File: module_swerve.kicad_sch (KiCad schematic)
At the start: 6 parts, among them J2 PlayingWFusion_CANDaisy_5-Link, M10 REV_NEO_Brushless_Motor, M11 REV_NEO_Brushless_Motor, U19 REV_Spark_MAX, U20 CTRE_CANCoder, U21 REV_Spark_MAX

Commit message: v1.2: added photoelectric sensor labels
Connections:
- new net: M11. (IN_C), U21. (VIN-)
- new net: M10. (IN_C), U19. (VIN-)
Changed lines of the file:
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@@
   (title_block
     (title "Schéma de câblage Disc-O 2024")
-    (date "2024-02-04")
-    (rev "1.1")
+    (date "2024-02-06")
+    (rev "1.2")
     (company "ASTRO 7605 (2024)")
   )

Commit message: Modify some fuses to 40A
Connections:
- new net: M11. (IN_C), U21. (VIN-)
- new net: M10. (IN_C), U19. (VIN-)
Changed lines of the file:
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@@
   (title_block
     (title "Schéma de câblage Disc-O 2024")
-    (date "2024-02-06")
-    (rev "1.2")
+    (date "2024-02-12")
+    (rev "1.4")
     (company "ASTRO 7605 (2024)")
   )

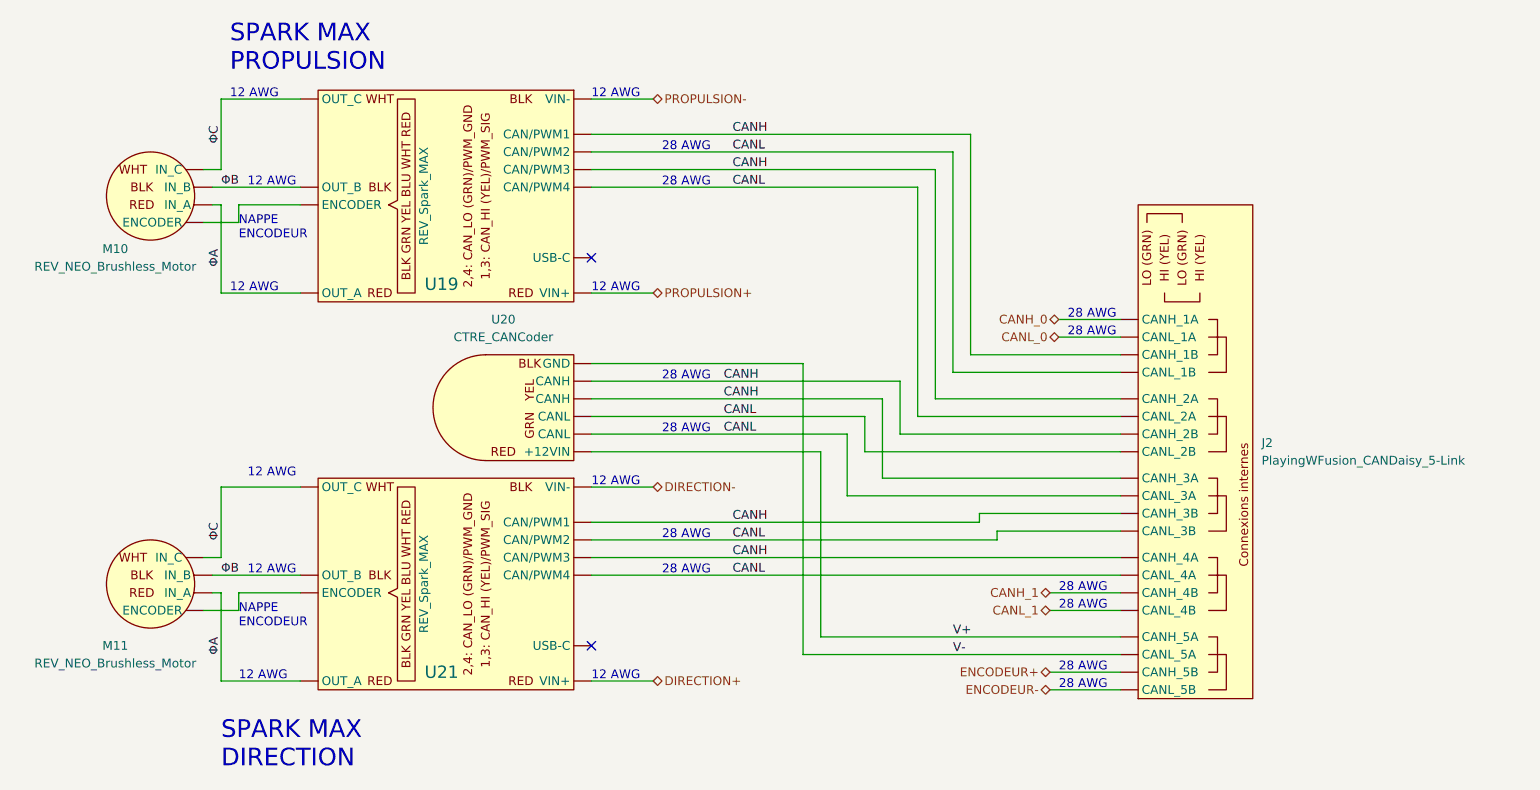
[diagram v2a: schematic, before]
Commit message: Ajout Orange Pi + sous-systeme vision
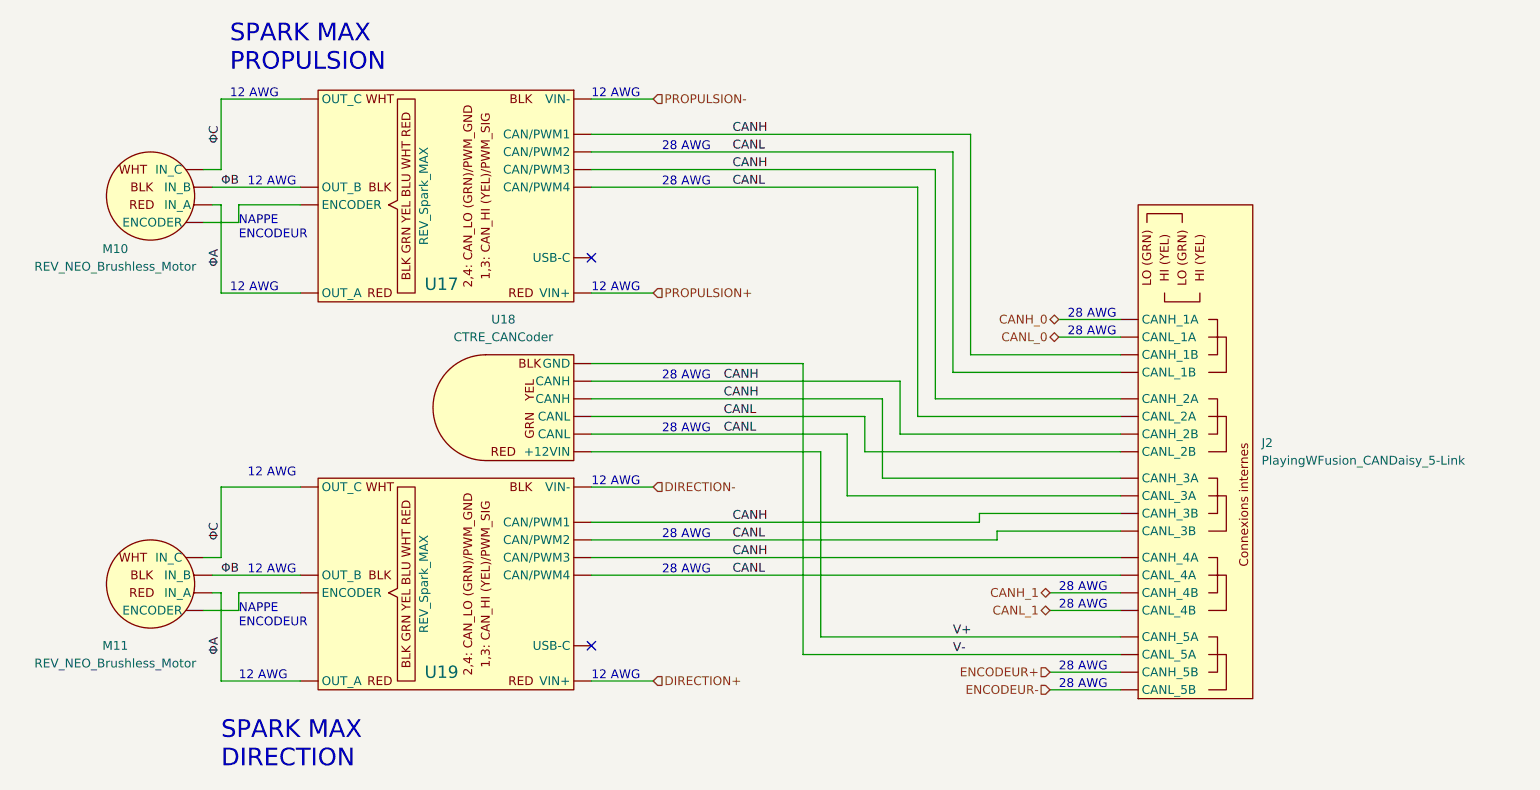
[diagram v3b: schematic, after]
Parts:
- renumbered U19 to U17, U20 to U18, U21 to U19
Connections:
- new net: M11. (IN_C), U19. (VIN-)
- new net: M10. (IN_C), U17. (VIN-)
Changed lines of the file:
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@@
   (title_block
     (title "Schéma de câblage Disc-O 2024")
-    (date "2024-02-12")
-    (rev "1.4")
+    (date "2024-02-17")
+    (rev "1.5")
     (company "ASTRO 7605 (2024)")
   )
@@
     (effects (font (size 1.27 1.27)) (justify left bottom))
   )
-  (hierarchical_label "ENCODEUR+" (shape bidirectional) (at 184.15 120.65 180) (fields_autoplaced)
+  (hierarchical_label "ENCODEUR+" (shape input) (at 184.15 120.65 180) (fields_autoplaced)
     (effects (font (size 1.27 1.27)) (justify right))
   )
-  (hierarchical_label "DIRECTION+" (shape bidirectional) (at 127 121.92 0) (fields_autoplaced)
+  (hierarchical_label "DIRECTION+" (shape input) (at 127 121.92 0) (fields_autoplaced)
     (effects (font (size 1.27 1.27)) (justify left))
   )
-  (hierarchical_label "PROPULSION+" (shape bidirectional) (at 127 66.04 0) (fields_autoplaced)
+  (hierarchical_label "PROPULSION+" (shape input) (at 127 66.04 0) (fields_autoplaced)
     (effects (font (size 1.27 1.27)) (justify left))
   )
@@
     (effects (font (size 1.27 1.27)) (justify right))
   )
-  (hierarchical_label "ENCODEUR-" (shape bidirectional) (at 184.15 123.19 180) (fields_autoplaced)
+  (hierarchical_label "ENCODEUR-" (shape input) (at 184.15 123.19 180) (fields_autoplaced)
     (effects (font (size 1.27 1.27)) (justify right))
   )
-  (hierarchical_label "PROPULSION-" (shape bidirectional) (at 127 38.1 0) (fields_autoplaced)
+  (hierarchical_label "PROPULSION-" (shape input) (at 127 38.1 0) (fields_autoplaced)
     (effects (font (size 1.27 1.27)) (justify left))
   )
-  (hierarchical_label "DIRECTION-" (shape bidirectional) (at 127 93.98 0) (fields_autoplaced)
+  (hierarchical_label "DIRECTION-" (shape input) (at 127 93.98 0) (fields_autoplaced)
     (effects (font (size 1.27 1.27)) (justify left))
   )
   (symbol (lib_id "FRC_Components:CTRE_CANCoder") (at 96.52 82.55 90) (unit 1)
     (in_bom yes) (on_board yes) (dnp no)
-    (property "Reference" "U20" (at 105.4294 69.85 90)
+    (property "Reference" "U18" (at 105.4294 69.85 90)
       (effects (font (size 1.27 1.27)))
     )
@@
       (project "schema_cablage_2024"
         (path "/e63e39d7-6ac0-4ffd-8aa3-1841a4541b55/b632b64e-d5b7-456d-a7ae-6969aba14a97"
-          (reference "U20") (unit 1)
+          (reference "U18") (unit 1)
         )
         (path "/e63e39d7-6ac0-4ffd-8aa3-1841a4541b55/e92e2da7-8df4-42ea-b0b1-e2a2f3556d07"
-          (reference "U29") (unit 1)
+          (reference "U27") (unit 1)
         )
         (path "/e63e39d7-6ac0-4ffd-8aa3-1841a4541b55/e4b49782-05fc-4e80-9ba9-edd7f0cdce32"
-          (reference "U23") (unit 1)
+          (reference "U21") (unit 1)
         )
         (path "/e63e39d7-6ac0-4ffd-8aa3-1841a4541b55/3439eb03-35bd-48b7-a9f1-5d73cc12bdd7"
-          (reference "U26") (unit 1)
+          (reference "U24") (unit 1)
         )
       )
@@
       (effects (font (size 1.27 1.27)) hide)
     )
-    (property "Datasheet" "" (at 69.85 107.95 0)
+    (property "Datasheet" "https://www.revrobotics.com/rev-21-1650/" (at 69.85 107.95 0)
       (effects (font (size 1.27 1.27)) hide)
     )
@@
   (symbol (lib_id "FRC_Components:REV_Spark_MAX") (at 96.52 52.07 270) (unit 1)
     (in_bom yes) (on_board yes) (dnp no)
-    (property "Reference" "U19" (at 96.52 64.77 90)
+    (property "Reference" "U17" (at 96.52 64.77 90)
       (effects (font (size 1.778 1.778)))
     )
@@
       (effects (font (size 1.27 1.27)) hide)
     )
-    (property "Datasheet" "" (at 96.52 52.07 0)
+    (property "Datasheet" "https://docs.revrobotics.com/brushless/spark-max/overview" (at 96.52 52.07 0)
+      (effects (font (size 1.27 1.27)) hide)
+    )
+    (pin "")
+    (pin "")
+    (pin "")
+    (pin "")
+    (pin "")
+    (pin "")
+    (pin "")
+    (pin "")
+    (pin "")
+    (pin "")
+    (pin "")
+    (instances
+      (project "schema_cablage_2024"
+        (path "/e63e39d7-6ac0-4ffd-8aa3-1841a4541b55/b632b64e-d5b7-456d-a7ae-6969aba14a97"
+          (reference "U17") (unit 1)
+        )
+        (path "/e63e39d7-6ac0-4ffd-8aa3-1841a4541b55/e4b49782-05fc-4e80-9ba9-edd7f0cdce32"
+          (reference "U20") (unit 1)
+        )
+        (path "/e63e39d7-6ac0-4ffd-8aa3-1841a4541b55/3439eb03-35bd-48b7-a9f1-5d73cc12bdd7"
+          (reference "U23") (unit 1)
+        )
+        (path "/e63e39d7-6ac0-4ffd-8aa3-1841a4541b55/e92e2da7-8df4-42ea-b0b1-e2a2f3556d07"
+          (reference "U26") (unit 1)
+        )
+      )
+    )
+  )
+  (symbol (lib_id "FRC_Components:REV_Spark_MAX") (at 96.52 107.95 270) (unit 1)
+    (in_bom yes) (on_board yes) (dnp no)
+    (property "Reference" "U19" (at 96.52 120.65 90)
+      (effects (font (size 1.778 1.778)))
+    )
+    (property "Value" "REV_Spark_MAX" (at 93.98 107.95 0)
+      (effects (font (size 1.27 1.27)))
+    )
+    (property "Footprint" "" (at 96.52 107.95 0)
+      (effects (font (size 1.27 1.27)) hide)
+    )
+    (property "Datasheet" "https://docs.revrobotics.com/brushless/spark-max/overview" (at 96.52 107.95 0)
       (effects (font (size 1.27 1.27)) hide)
     )
@@
     )
   )
-  (symbol (lib_id "FRC_Components:REV_Spark_MAX") (at 96.52 107.95 270) (unit 1)
-    (in_bom yes) (on_board yes) (dnp no)
-    (property "Reference" "U21" (at 96.52 120.65 90)
-      (effects (font (size 1.778 1.778)))
-    )
-    (property "Value" "REV_Spark_MAX" (at 93.98 107.95 0)
-      (effects (font (size 1.27 1.27)))
-    )
-    (property "Footprint" "" (at 96.52 107.95 0)
-      (effects (font (size 1.27 1.27)) hide)
-    )
-    (property "Datasheet" "" (at 96.52 107.95 0)
-      (effects (font (size 1.27 1.27)) hide)
-    )
-    (pin "")
-    (pin "")
-    (pin "")
-    (pin "")
-    (pin "")
-    (pin "")
-    (pin "")
-    (pin "")
-    (pin "")
-    (pin "")
-    (pin "")
-    (instances
-      (project "schema_cablage_2024"
-        (path "/e63e39d7-6ac0-4ffd-8aa3-1841a4541b55/b632b64e-d5b7-456d-a7ae-6969aba14a97"
-          (reference "U21") (unit 1)
-        )
-        (path "/e63e39d7-6ac0-4ffd-8aa3-1841a4541b55/e4b49782-05fc-4e80-9ba9-edd7f0cdce32"
-          (reference "U24") (unit 1)
-        )
-        (path "/e63e39d7-6ac0-4ffd-8aa3-1841a4541b55/3439eb03-35bd-48b7-a9f1-5d73cc12bdd7"
-          (reference "U27") (unit 1)
-        )
-        (path "/e63e39d7-6ac0-4ffd-8aa3-1841a4541b55/e92e2da7-8df4-42ea-b0b1-e2a2f3556d07"
-          (reference "U30") (unit 1)
-        )
-      )
-    )
-  )
   (symbol (lib_id "FRC_Components:PlayingWFusion_CANDaisy_5-Link") (at 187.96 88.9 90) (unit 1)
     (in_bom yes) (on_board yes) (dnp no) (fields_autoplaced)
@@
       (effects (font (size 1.27 1.27)) hide)
     )
-    (property "Datasheet" "" (at 69.85 52.07 0)
-      (effects (font (size 1.27 1.27)) hide)
-    )
+    (property "Datasheet" "https://www.revrobotics.com/rev-21-1650/" (at 69.85 52.07 0)
+      (effects (font (size 1.27 1.27)) hide)
+    )

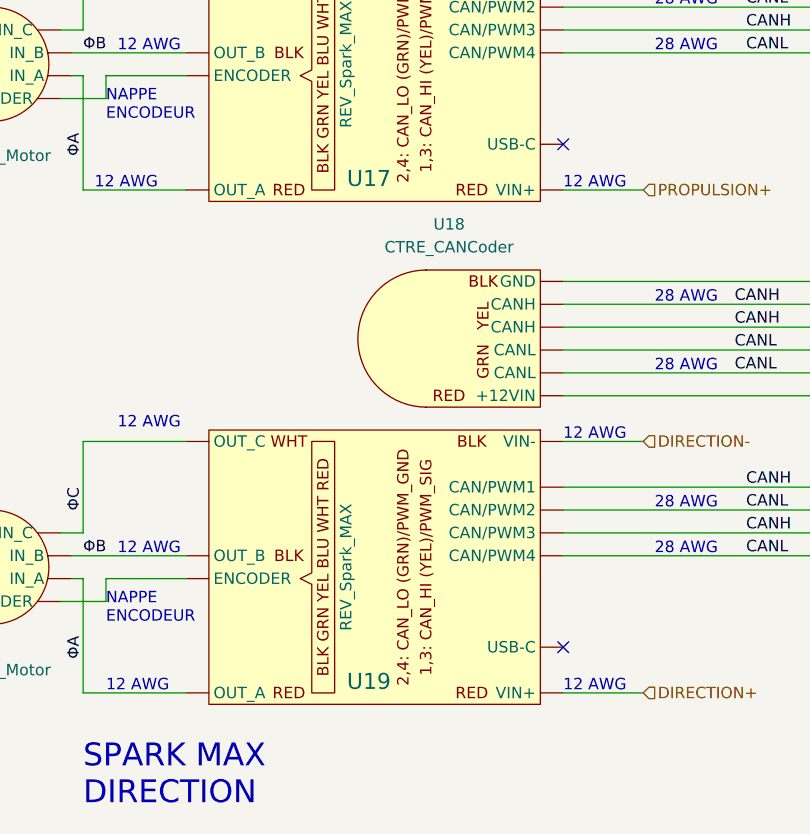
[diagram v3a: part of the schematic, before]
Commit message: Ajout Limelight + webcam
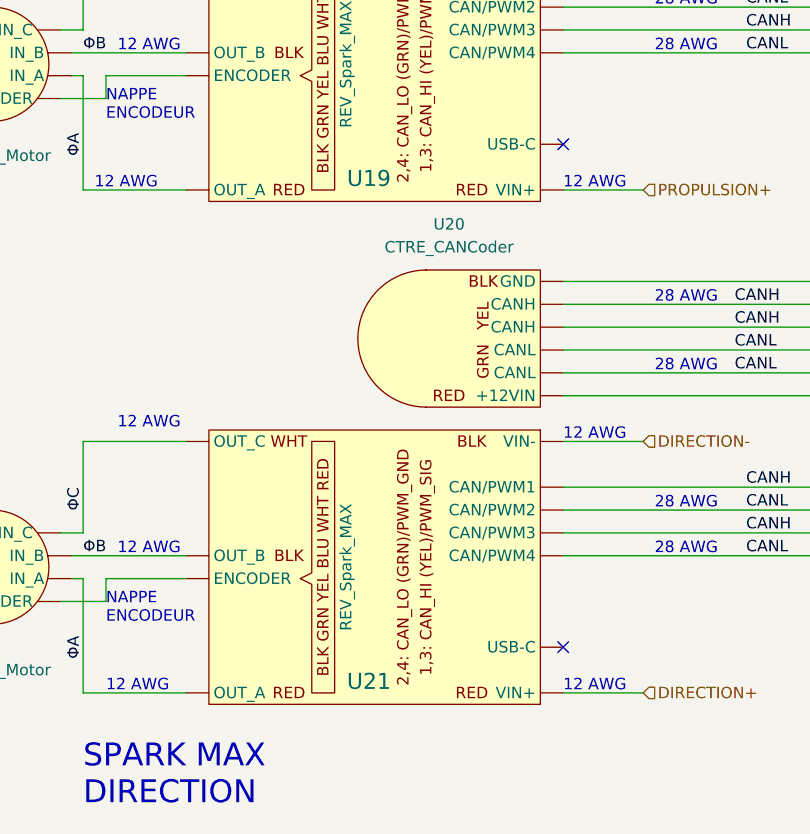
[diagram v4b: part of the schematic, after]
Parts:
- renumbered U17 to U19, U18 to U20, U19 to U21
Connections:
- new net: M11. (IN_C), U21. (VIN-)
- new net: M10. (IN_C), U19. (VIN-)
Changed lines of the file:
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@@
   (title_block
     (title "Schéma de câblage Disc-O 2024")
-    (date "2024-02-17")
-    (rev "1.5")
+    (date "2024-02-27")
+    (rev "1.6")
     (company "ASTRO 7605 (2024)")
   )
@@
   (symbol (lib_id "FRC_Components:CTRE_CANCoder") (at 96.52 82.55 90) (unit 1)
     (in_bom yes) (on_board yes) (dnp no)
-    (property "Reference" "U18" (at 105.4294 69.85 90)
+    (property "Reference" "U20" (at 105.4294 69.85 90)
       (effects (font (size 1.27 1.27)))
     )
@@
       (project "schema_cablage_2024"
         (path "/e63e39d7-6ac0-4ffd-8aa3-1841a4541b55/b632b64e-d5b7-456d-a7ae-6969aba14a97"
-          (reference "U18") (unit 1)
+          (reference "U20") (unit 1)
         )
         (path "/e63e39d7-6ac0-4ffd-8aa3-1841a4541b55/e92e2da7-8df4-42ea-b0b1-e2a2f3556d07"
-          (reference "U27") (unit 1)
+          (reference "U29") (unit 1)
         )
         (path "/e63e39d7-6ac0-4ffd-8aa3-1841a4541b55/e4b49782-05fc-4e80-9ba9-edd7f0cdce32"
-          (reference "U21") (unit 1)
+          (reference "U23") (unit 1)
         )
         (path "/e63e39d7-6ac0-4ffd-8aa3-1841a4541b55/3439eb03-35bd-48b7-a9f1-5d73cc12bdd7"
-          (reference "U24") (unit 1)
+          (reference "U26") (unit 1)
         )
       )
@@
   (symbol (lib_id "FRC_Components:REV_Spark_MAX") (at 96.52 52.07 270) (unit 1)
     (in_bom yes) (on_board yes) (dnp no)
-    (property "Reference" "U17" (at 96.52 64.77 90)
+    (property "Reference" "U19" (at 96.52 64.77 90)
       (effects (font (size 1.778 1.778)))
     )
@@
     )
     (property "Datasheet" "https://docs.revrobotics.com/brushless/spark-max/overview" (at 96.52 52.07 0)
-      (effects (font (size 1.27 1.27)) hide)
-    )
-    (pin "")
-    (pin "")
-    (pin "")
-    (pin "")
-    (pin "")
-    (pin "")
-    (pin "")
-    (pin "")
-    (pin "")
-    (pin "")
-    (pin "")
-    (instances
-      (project "schema_cablage_2024"
-        (path "/e63e39d7-6ac0-4ffd-8aa3-1841a4541b55/b632b64e-d5b7-456d-a7ae-6969aba14a97"
-          (reference "U17") (unit 1)
-        )
-        (path "/e63e39d7-6ac0-4ffd-8aa3-1841a4541b55/e4b49782-05fc-4e80-9ba9-edd7f0cdce32"
-          (reference "U20") (unit 1)
-        )
-        (path "/e63e39d7-6ac0-4ffd-8aa3-1841a4541b55/3439eb03-35bd-48b7-a9f1-5d73cc12bdd7"
-          (reference "U23") (unit 1)
-        )
-        (path "/e63e39d7-6ac0-4ffd-8aa3-1841a4541b55/e92e2da7-8df4-42ea-b0b1-e2a2f3556d07"
-          (reference "U26") (unit 1)
-        )
-      )
-    )
-  )
-  (symbol (lib_id "FRC_Components:REV_Spark_MAX") (at 96.52 107.95 270) (unit 1)
-    (in_bom yes) (on_board yes) (dnp no)
-    (property "Reference" "U19" (at 96.52 120.65 90)
-      (effects (font (size 1.778 1.778)))
-    )
-    (property "Value" "REV_Spark_MAX" (at 93.98 107.95 0)
-      (effects (font (size 1.27 1.27)))
-    )
-    (property "Footprint" "" (at 96.52 107.95 0)
-      (effects (font (size 1.27 1.27)) hide)
-    )
-    (property "Datasheet" "https://docs.revrobotics.com/brushless/spark-max/overview" (at 96.52 107.95 0)
       (effects (font (size 1.27 1.27)) hide)
     )
@@
         )
       )
+    )
+  )
+  (symbol (lib_id "FRC_Components:REV_Spark_MAX") (at 96.52 107.95 270) (unit 1)
+    (in_bom yes) (on_board yes) (dnp no)
+    (property "Reference" "U21" (at 96.52 120.65 90)
+      (effects (font (size 1.778 1.778)))
+    )
+    (property "Value" "REV_Spark_MAX" (at 93.98 107.95 0)
+      (effects (font (size 1.27 1.27)))
+    )
+    (property "Footprint" "" (at 96.52 107.95 0)
+      (effects (font (size 1.27 1.27)) hide)
+    )
+    (property "Datasheet" "https://docs.revrobotics.com/brushless/spark-max/overview" (at 96.52 107.95 0)
+      (effects (font (size 1.27 1.27)) hide)
+    )
+    (pin "")
+    (pin "")
+    (pin "")
+    (pin "")
+    (pin "")
+    (pin "")
+    (pin "")
+    (pin "")
+    (pin "")
+    (pin "")
+    (pin "")
+    (instances
+      (project "schema_cablage_2024"
+        (path "/e63e39d7-6ac0-4ffd-8aa3-1841a4541b55/b632b64e-d5b7-456d-a7ae-6969aba14a97"
+          (reference "U21") (unit 1)
+        )
+        (path "/e63e39d7-6ac0-4ffd-8aa3-1841a4541b55/e4b49782-05fc-4e80-9ba9-edd7f0cdce32"
+          (reference "U24") (unit 1)
+        )
+        (path "/e63e39d7-6ac0-4ffd-8aa3-1841a4541b55/3439eb03-35bd-48b7-a9f1-5d73cc12bdd7"
+          (reference "U27") (unit 1)
+        )
+        (path "/e63e39d7-6ac0-4ffd-8aa3-1841a4541b55/e92e2da7-8df4-42ea-b0b1-e2a2f3556d07"
+          (reference "U30") (unit 1)
+        )
+      )

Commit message: Remove rogue no-connects, update to KiCad 8.0
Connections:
- new net: M11. (IN_C), U21. (VIN-)
- new net: M10. (IN_C), U19. (VIN-)

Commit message: Added Coral
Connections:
- new net: M11. (IN_C), U21. (VIN-)
- new net: M10. (IN_C), U19. (VIN-)
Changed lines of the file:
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@@
 	(title_block
 		(title "Schéma de câblage Disc-O 2024")
-		(date "2024-02-27")
-		(rev "1.6")
+		(date "2024-03-09")
+		(rev "1.7")
 		(company "ASTRO 7605 (2024)")
 	)
@@
 			)
 		)
-		(property "Description" ""
+		(property "Description" "Cross The Road Electronics CAN absolute encoder"
 			(at 96.52 82.55 0)
 			(effects
@@
 			)
 		)
-		(property "Description" ""
+		(property "Description" "NEO Brushless Motor for First Robotics, REV Robotics"
 			(at 69.85 107.95 0)
 			(effects
@@
 			)
 		)
-		(property "Description" ""
+		(property "Description" "Spark MAX ESC for First Robotics, REV Robotics"
 			(at 96.52 52.07 0)
 			(effects
@@
 	)
 	(symbol
+		(lib_name "FRC_Components:REV_Spark_MAX")
 		(lib_id "FRC_Components:REV_Spark_MAX")
 		(at 96.52 107.95 270)
@@
 			)
 		)
-		(property "Description" ""
+		(property "Description" "Spark MAX ESC for First Robotics, REV Robotics"
 			(at 96.52 107.95 0)
 			(effects
@@
 			)
 		)
-		(property "Description" ""
+		(property "Description" "Playing With Fusion CAN daisy chain connector board, 5x2 pairs"
 			(at 187.96 88.9 0)
 			(effects
@@
 	)
 	(symbol
+		(lib_name "FRC_Components:REV_NEO_Brushless_Motor")
 		(lib_id "FRC_Components:REV_NEO_Brushless_Motor")
 		(at 69.85 52.07 270)
@@
 			)
 		)
-		(property "Description" ""
+		(property "Description" "NEO Brushless Motor for First Robotics, REV Robotics"
 			(at 69.85 52.07 0)
 			(effects
